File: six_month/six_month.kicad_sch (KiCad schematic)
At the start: 0 parts

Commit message: WIP: Updated Software Design Block
Starting brainstorming the software integration. Starting High level conceptual, then moving more low level and subprocesses come to mind.
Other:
- added sheet DAC and Aux (DAC.kicad_sch)
- note added: "Append"
- note added: "Bluetooth"
- note added: "I2C"
- note added: "I2S"
- note added: "Init"
- note added: "Main"
- note added: "Media Web Server"
- note added: "Stereo Speakers (End User)"
- note added: "WIFI"
- note removed: "I2C0"

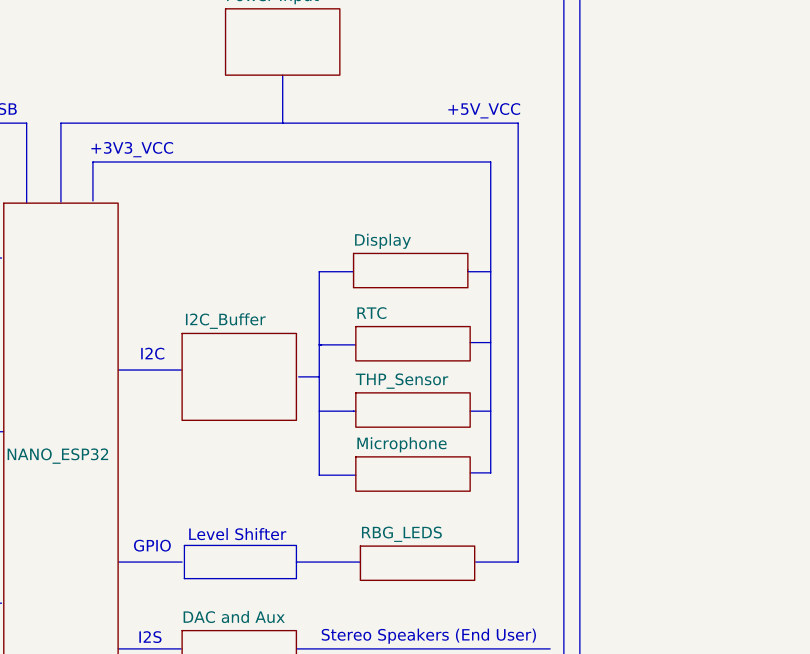
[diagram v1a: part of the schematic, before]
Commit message: Changes
Removed the microphone idea, added a DAC for Bluetooth to Line out. Allows for external speakers to be connected via an Aux cable
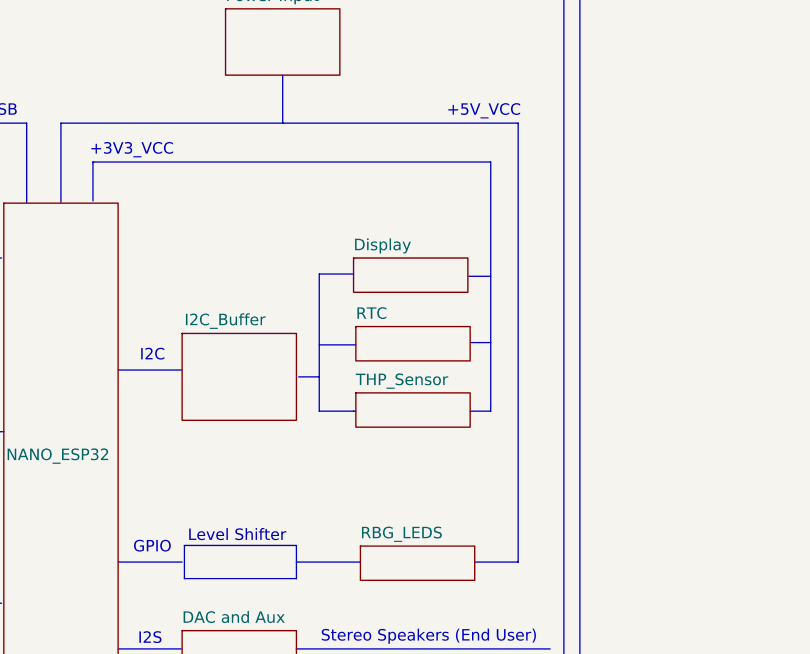
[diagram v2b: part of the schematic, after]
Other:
- removed sheet Microphone

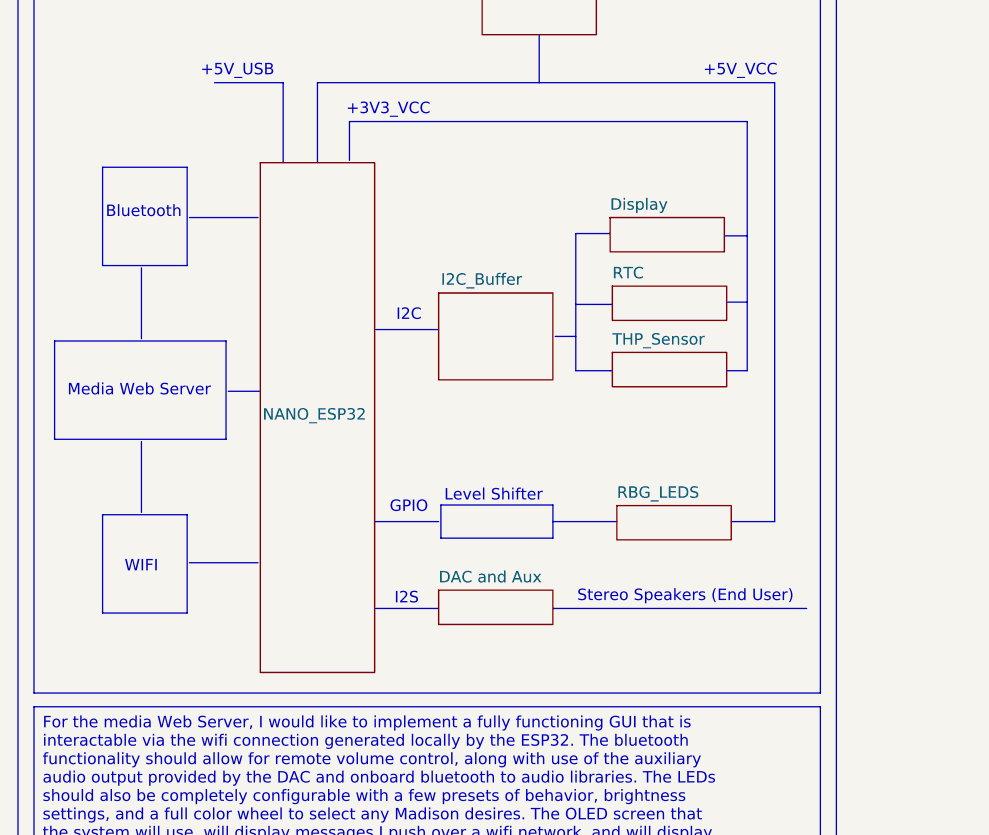
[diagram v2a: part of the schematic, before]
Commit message: Removed some stuff
Removed the speaker stuff because we dont need it.
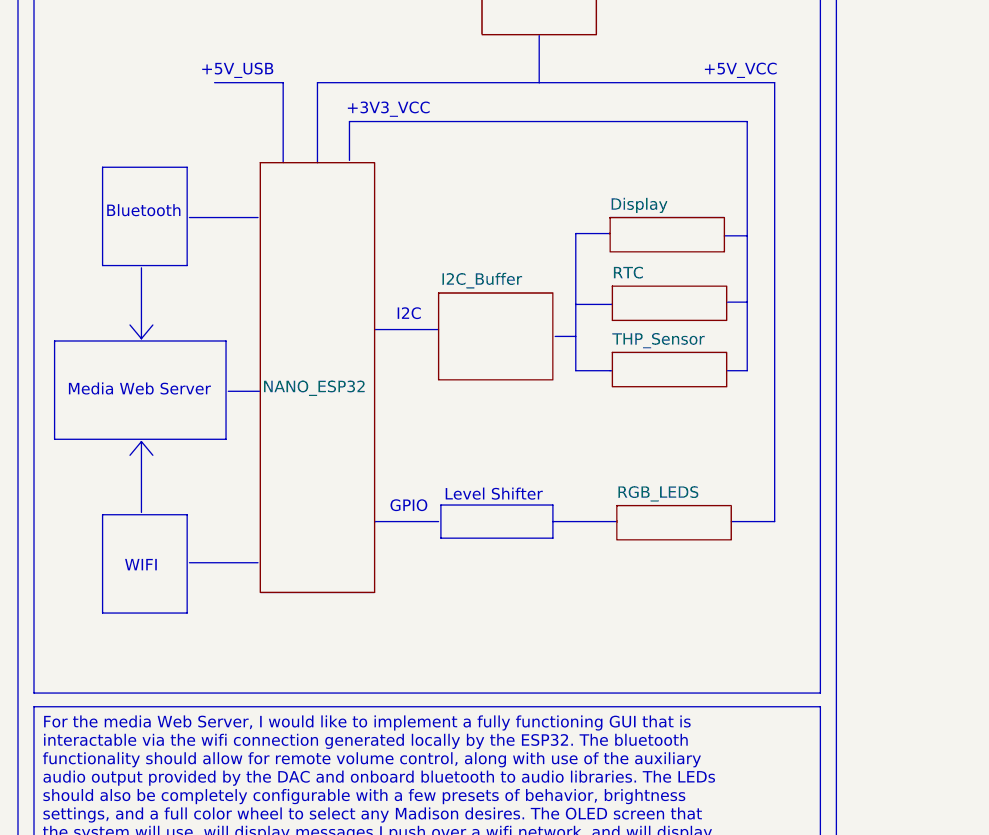
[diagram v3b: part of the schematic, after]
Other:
- sheet RBG_LEDS renamed RGB_LEDS
- removed sheet DAC and Aux
- note removed: "I2S"
- note removed: "Stereo Speakers (End User)"
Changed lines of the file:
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@@
-		)
-	)
-	(text "I2S"
-		(exclude_from_sim no)
-		(at 55.88 149.606 0)
-		(effects
-			(font
-				(size 1.27 1.27)
-			)
 		)
 	)
@@
 			(font
 				(size 2.54 2.54)
-			)
-		)
-	)
-	(text "Stereo Speakers (End User)"
-		(exclude_from_sim no)
-		(at 86.868 149.352 0)
-		(effects
-			(font
-				(size 1.27 1.27)
 			)
 		)
@@
 	(polyline
 		(pts
-			(xy 52.324 150.622) (xy 59.436 150.622)
-		)
-		(stroke
-			(width 0)
-			(type solid)
-			(color 255 255 0 1)
-		)
-	)
-	(polyline
-		(pts
 			(xy 74.676 108.966) (xy 74.676 124.206)
 		)
@@
 	(polyline
 		(pts
+			(xy 26.416 120.65) (xy 27.686 119.126)
+		)
+		(stroke
+			(width 0)
+			(type solid)
+			(color 255 255 255 1)
+		)
+	)
+	(polyline
+		(pts
 			(xy 36.068 126.492) (xy 39.624 126.492)
 		)
@@
 	(polyline
 		(pts
+			(xy 26.416 132.08) (xy 25.146 133.604)
+		)
+		(stroke
+			(width 0)
+			(type solid)
+			(color 255 255 255 1)
+		)
+	)
+	(polyline
+		(pts
 			(xy 52.324 140.97) (xy 59.436 140.97)
 		)
@@
 	(polyline
 		(pts
-			(xy 72.136 150.622) (xy 100.33 150.622)
-		)
-		(stroke
-			(width 0)
-			(type solid)
-			(color 255 255 0 1)
-		)
-	)
-	(polyline
-		(pts
 			(xy 34.544 92.202) (xy 42.164 92.202)
 		)
@@
 		(pts
 			(xy 31.75 145.542) (xy 39.37 145.542)
+		)
+		(stroke
+			(width 0)
+			(type solid)
+			(color 255 255 255 1)
+		)
+	)
+	(polyline
+		(pts
+			(xy 26.416 120.65) (xy 25.146 119.126)
+		)
+		(stroke
+			(width 0)
+			(type solid)
+			(color 255 255 255 1)
+		)
+	)
+	(polyline
+		(pts
+			(xy 26.416 132.08) (xy 27.686 133.604)
 		)
 		(stroke
@@
 	)
 	(sheet
-		(at 59.436 148.59)
+		(at 78.74 122.174)
 		(size 12.7 3.81)
 		(exclude_from_sim no)
@@
 			(color 0 0 0 0.0000)
 		)
-		(property "Sheetname" "DAC and Aux"
-			(at 59.436 147.8784 0)
+		(property "Sheetname" "THP_Sensor"
+			(at 78.74 121.4624 0)
 			(effects
 				(font
@@
 			)
 		)
-		(property "Sheetfile" "DAC.kicad_sch"
-			(at 59.436 152.9846 0)
+		(property "Sheetfile" "temp.kicad_sch"
+			(at 78.74 126.5686 0)
 			(effects
 				(font
@@
 			(project "six_month"
 				(path "/760b3a53-058c-44df-84b8-d25bd41bf801"
-					(page "10")
+					(page "9")
 				)
 			)
@@
 	)
 	(sheet
-		(at 78.74 122.174)
-		(size 12.7 3.81)
+		(at 64.262 79.502)
+		(size 12.7 7.366)
 		(exclude_from_sim no)
 		(in_bom yes)
@@
 			(color 0 0 0 0.0000)
 		)
-		(property "Sheetname" "THP_Sensor"
-			(at 78.74 121.4624 0)
+		(property "Sheetname" "Power Input"
+			(at 64.262 78.7904 0)
 			(effects
 				(font
@@
 			)
 		)
-		(property "Sheetfile" "temp.kicad_sch"
-			(at 78.74 126.5686 0)
+		(property "Sheetfile" "Power Input.kicad_sch"
+			(at 64.262 87.4526 0)
 			(effects
 				(font
@@
 			(project "six_month"
 				(path "/760b3a53-058c-44df-84b8-d25bd41bf801"
-					(page "9")
+					(page "4")
 				)
 			)
@@
 	)
 	(sheet
-		(at 64.262 79.502)
-		(size 12.7 7.366)
+		(at 79.248 139.192)
+		(size 12.7 3.81)
 		(exclude_from_sim no)
 		(in_bom yes)
@@
 			(color 0 0 0 0.0000)
 		)
-		(property "Sheetname" "Power Input"
-			(at 64.262 78.7904 0)
+		(property "Sheetname" "RGB_LEDS"
+			(at 79.248 138.4804 0)
 			(effects
 				(font
@@
 			)
 		)
-		(property "Sheetfile" "Power Input.kicad_sch"
-			(at 64.262 87.4526 0)
+		(property "Sheetfile" "RBG_LEDS.kicad_sch"
+			(at 79.248 143.5866 0)
 			(effects
 				(font
@@
 			(project "six_month"
 				(path "/760b3a53-058c-44df-84b8-d25bd41bf801"
-					(page "4")
+					(page "7")
 				)
 			)
@@
 	)
 	(sheet
-		(at 79.248 139.192)
+		(at 78.486 107.188)
 		(size 12.7 3.81)
 		(exclude_from_sim no)
@@
 			(color 0 0 0 0.0000)
 		)
-		(property "Sheetname" "RBG_LEDS"
-			(at 79.248 138.4804 0)
-			(effects
-				(font
-					(size 1.27 1.27)
-				)
-				(justify left bottom)
-			)
-		)
-		(property "Sheetfile" "RBG_LEDS.kicad_sch"
-			(at 79.248 143.5866 0)
-			(effects
-				(font
-					(size 1.27 1.27)
-				)
-				(justify left top)
-				(hide yes)
-			)
-		)
-		(instances
-			(project "six_month"
-				(path "/760b3a53-058c-44df-84b8-d25bd41bf801"
-					(page "7")
-				)
-			)
-		)
-	)
-	(sheet
-		(at 78.486 107.188)
-		(size 12.7 3.81)
-		(exclude_from_sim no)
-		(in_bom yes)
-		(on_board yes)
-		(dnp no)
-		(fields_autoplaced yes)
-		(stroke
-			(width 0.1524)
-			(type solid)
-		)
-		(fill
-			(color 0 0 0 0.0000)
-		)
 		(property "Sheetname" "Display"
 			(at 78.486 106.4764 0)
@@
 	(sheet
 		(at 39.624 101.092)
-		(size 12.7 56.642)
+		(size 12.7 47.752)
 		(exclude_from_sim no)
 		(in_bom yes)
@@
 		)
 		(property "Sheetname" "NANO_ESP32"
-			(at 39.878 129.794 0)
-			(effects
-				(font
+			(at 39.878 126.746 0)
+			(effects
+				(font
